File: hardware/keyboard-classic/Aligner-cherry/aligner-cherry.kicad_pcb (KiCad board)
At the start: 2 copper layers, 312.4 x 118.1 mm, 77 parts, among them SW1 RT Arrow, SW10 Bracket_Open, SW11 6, SW12 Y, SW13 Return, SW14 Dash, SW15 5, SW16 T, SW17 Line Feed, SW18 Colon, SW19 4, SW2 LT Arrow, SW20 R, SW21 O, SW22 0, SW23 3, SW24 E, SW25 L, SW26 9, SW27 2, SW28 W, SW29 Period, SW3 Tilde, SW30 8, SW31 1, SW32 @ (AT), SW33 Break, SW34 Rubout, SW35 R_Shift, SW36 P, SW37 Comma, SW38 K, SW39 L_Shift, SW4 I, SW40 Semicolon, SW41 M, SW42 J, SW43 Fwd_Slash, SW44 N, SW45 H, SW46 SPACE, SW47 B, SW48 G, SW49 TAB, SW5 Repeat, SW50 Z, SW51 V, SW52 F, SW53 CTRL, SW54 A, SW55 C, SW56 D, SW57 Backslash, SW58 Q, SW59 X, SW6 Bracket_Close, SW60 S, SW61 FN, SW62 ESC, SW7 7, SW8 U, SW9 Caps Lock

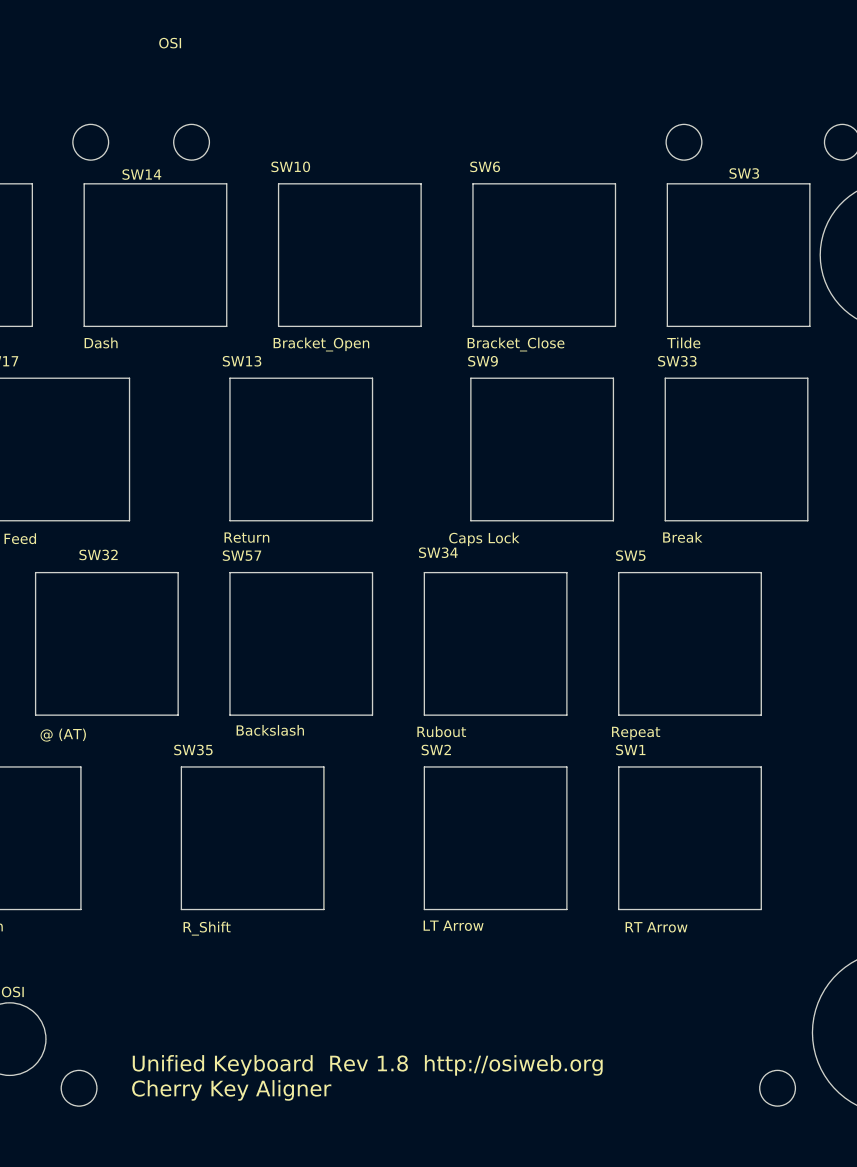
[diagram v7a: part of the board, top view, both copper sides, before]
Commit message: Adjust some holes so interface mount holes double as aligner mounts.
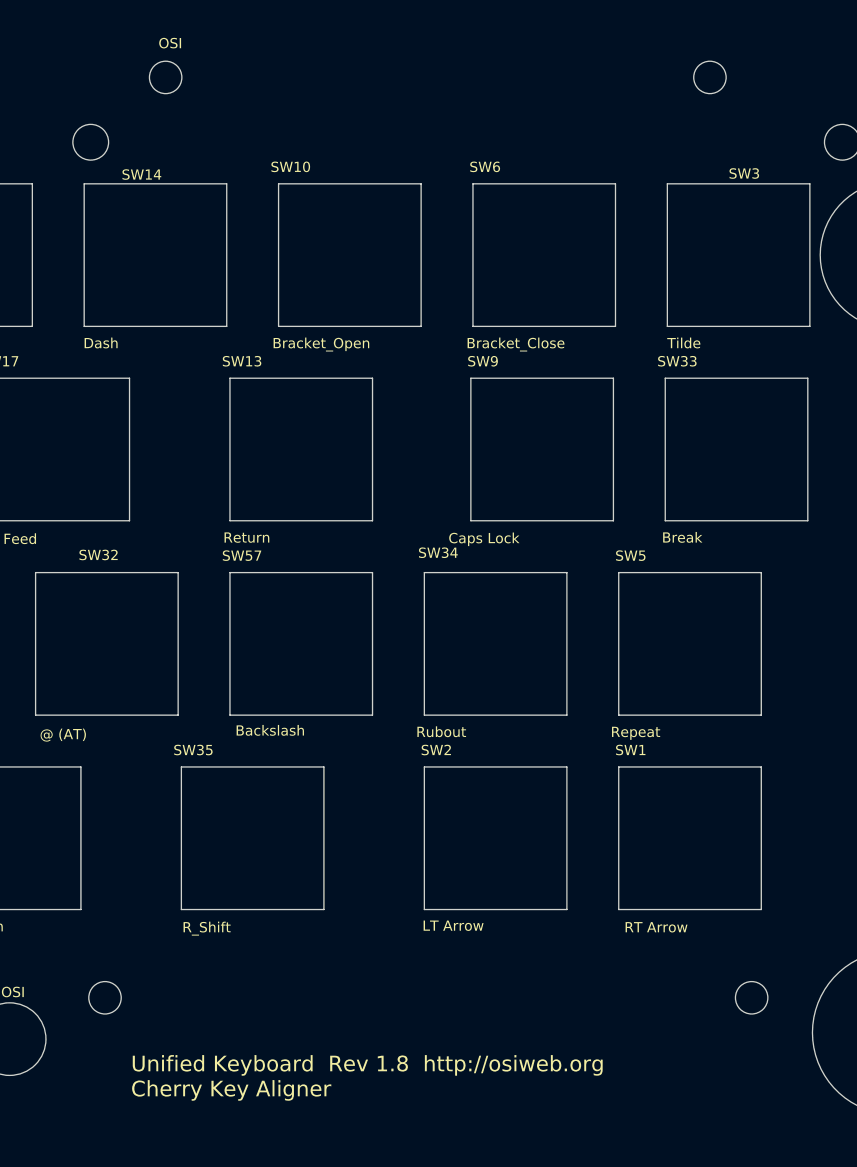
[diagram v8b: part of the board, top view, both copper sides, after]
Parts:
- removed the REF** at (349.0, 78.7)
- removed the REF** at (300.7, 78.7)
- removed the REF** at (358.1, 171.4)
- removed the REF** at (289.7, 171.4)
- added REF**: Interface mount, unikbd:kbd_mounting_holes_only, F.Cu at (301.0, 163.9)
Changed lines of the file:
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@@
     (tracks 0)
     (zones 0)
-    (modules 77)
+    (modules 74)
     (nets 1)
   )
@@
     (diff_pair_gap 0.254)
   )
+  (module unikbd:kbd_mounting_holes_only (layer F.Cu)
+    (at 301.0408 163.87826 90)
+    (descr "Through hole straight pin header, 2x20, 2.54mm pitch, double rows")
+    (tags "Through hole pin header THT 2x20 2.54mm double row")
+    (fp_text reference REF** (at 1.2954 -2.5078 90) (layer F.Fab) hide
+      (effects (font (size 1 1) (thickness 0.15)))
+    )
+    (fp_text value "Interface mount" (at 1.27 50.59 90) (layer F.Fab) hide
+      (effects (font (size 1 1) (thickness 0.15)))
+    )
+    (pad "" np_thru_hole circle (at 1.2954 54.5606 90) (size 3.175 3.175) (drill 3.175) (layers *.Cu *.Mask))
+    (pad "" np_thru_hole circle (at 1.2954 -8.8124 90) (size 3.175 3.175) (drill 3.175) (layers *.Cu *.Mask))
+    (pad "" np_thru_hole circle (at 91.4924 -2.8688 90) (size 3.175 3.175) (drill 3.175) (layers *.Cu *.Mask))
+    (pad "" np_thru_hole circle (at 91.4924 50.4712 90) (size 3.175 3.175) (drill 3.175) (layers *.Cu *.Mask))
+    (model ${KISYS3DMOD}/Connector_PinHeader_2.54mm.3dshapes/PinHeader_2x20_P2.54mm_Vertical.wrl
+      (offset (xyz 2.54 0 -1.8288))
+      (scale (xyz 1 1 1))
+      (rotate (xyz 0 180 0))
+    )
+  )
   (module unikbd:OSI_spacer_holes (layer F.Cu)
     (at 197.15988 165.99916)
@@
       (effects (font (size 1 1) (thickness 0.15)))
     )
+    (fp_line (start 104.14 -87.63) (end 104.14 -102.87) (layer F.CrtYd) (width 0.12))
+    (fp_line (start 104.14 -87.63) (end 114.3 -87.63) (layer F.CrtYd) (width 0.12))
+    (fp_line (start 114.3 -102.87) (end 114.3 -87.63) (layer F.CrtYd) (width 0.12))
+    (fp_line (start 104.14 -102.87) (end 114.3 -102.87) (layer F.CrtYd) (width 0.12))
+    (fp_line (start -114.3 -87.63) (end -114.3 -102.87) (layer F.CrtYd) (width 0.12))
+    (fp_line (start -114.3 -87.63) (end -104.14 -87.63) (layer F.CrtYd) (width 0.12))
+    (fp_line (start -104.14 -102.87) (end -104.14 -87.63) (layer F.CrtYd) (width 0.12))
+    (fp_line (start -114.3 -102.87) (end -104.14 -102.87) (layer F.CrtYd) (width 0.12))
+    (fp_line (start -5.08 -87.7824) (end -5.08 -103.0224) (layer F.CrtYd) (width 0.12))
+    (fp_line (start -5.08 -87.7824) (end 5.08 -87.7824) (layer F.CrtYd) (width 0.12))
+    (fp_line (start 5.08 -103.0224) (end 5.08 -87.7824) (layer F.CrtYd) (width 0.12))
+    (fp_line (start -5.08 -103.0224) (end 5.08 -103.0224) (layer F.CrtYd) (width 0.12))
+    (fp_circle (center 109.22 -97.79) (end 114.046 -97.79) (layer Cmts.User) (width 0.15))
+    (fp_circle (center -109.22 -97.79) (end -104.394 -97.79) (layer Cmts.User) (width 0.15))
+    (fp_circle (center 0 -97.9424) (end 4.826 -97.9424) (layer Cmts.User) (width 0.15))
+    (fp_circle (center -85.725 0.635) (end -81.975 0.635) (layer F.CrtYd) (width 0.05))
+    (fp_circle (center -85.725 0.635) (end -82.225 0.635) (layer Cmts.User) (width 0.15))
+    (fp_circle (center 85.725 0.635) (end 89.475 0.635) (layer F.CrtYd) (width 0.05))
+    (fp_circle (center 85.725 0.635) (end 89.225 0.635) (layer Cmts.User) (width 0.15))
+    (fp_circle (center 0 -92.8624) (end 4.826 -92.8624) (layer Cmts.User) (width 0.15))
+    (fp_circle (center -109.22 -92.71) (end -104.394 -92.71) (layer Cmts.User) (width 0.15))
     (fp_circle (center 109.22 -92.71) (end 114.046 -92.71) (layer Cmts.User) (width 0.15))
-    (fp_circle (center 109.22 -92.71) (end 114.3 -92.71) (layer F.CrtYd) (width 0.05))
-    (fp_circle (center -109.22 -92.71) (end -104.394 -92.71) (layer Cmts.User) (width 0.15))
-    (fp_circle (center -109.22 -92.71) (end -104.14 -92.71) (layer F.CrtYd) (width 0.05))
-    (fp_circle (center 0 -92.8624) (end 4.826 -92.8624) (layer Cmts.User) (width 0.15))
-    (fp_circle (center 0 -92.8624) (end 5.08 -92.8624) (layer F.CrtYd) (width 0.05))
-    (fp_circle (center 85.725 0.635) (end 89.225 0.635) (layer Cmts.User) (width 0.15))
-    (fp_circle (center 85.725 0.635) (end 89.475 0.635) (layer F.CrtYd) (width 0.05))
-    (fp_circle (center -85.725 0.635) (end -82.225 0.635) (layer Cmts.User) (width 0.15))
-    (fp_circle (center -85.725 0.635) (end -81.975 0.635) (layer F.CrtYd) (width 0.05))
-    (fp_circle (center 0 -97.9424) (end 4.826 -97.9424) (layer Cmts.User) (width 0.15))
-    (fp_circle (center 0 -97.9424) (end 5.08 -97.9424) (layer F.CrtYd) (width 0.05))
-    (fp_circle (center -109.22 -97.79) (end -104.394 -97.79) (layer Cmts.User) (width 0.15))
-    (fp_circle (center -109.22 -97.79) (end -104.14 -97.79) (layer F.CrtYd) (width 0.05))
-    (fp_circle (center 109.22 -97.79) (end 114.046 -97.79) (layer Cmts.User) (width 0.15))
-    (fp_circle (center 109.22 -97.79) (end 114.3 -97.79) (layer F.CrtYd) (width 0.05))
     (fp_text user %R (at 110.75162 -87.97036) (layer F.Fab)
       (effects (font (size 1 1) (thickness 0.15)))
@@
   )
   (module MountingHole:MountingHole_3.5mm (layer F.Cu)
-    (at 358.14 171.45)
-    (descr "Mounting Hole 3.5mm, no annular")
-    (tags "mounting hole 3.5mm no annular")
-    (attr virtual)
-    (fp_text reference REF** (at 0 -4.5) (layer F.SilkS) hide
-      (effects (font (size 1 1) (thickness 0.15)))
-    )
-    (fp_text value MountingHole_3.5mm (at 0 4.5) (layer F.Fab) hide
-      (effects (font (size 1 1) (thickness 0.15)))
-    )
-    (fp_circle (center 0 0) (end 3.5 0) (layer Cmts.User) (width 0.15))
-    (fp_circle (center 0 0) (end 3.75 0) (layer F.CrtYd) (width 0.05))
-    (fp_text user %R (at 0.3 0) (layer F.Fab) hide
-      (effects (font (size 1 1) (thickness 0.15)))
-    )
-    (pad 1 np_thru_hole circle (at 0 0) (size 3.5 3.5) (drill 3.5) (layers *.Cu *.Mask))
-  )
-  (module MountingHole:MountingHole_3.5mm (layer F.Cu)
-    (at 289.687 171.45)
-    (descr "Mounting Hole 3.5mm, no annular")
-    (tags "mounting hole 3.5mm no annular")
-    (attr virtual)
-    (fp_text reference REF** (at 0 -4.5) (layer F.SilkS) hide
-      (effects (font (size 1 1) (thickness 0.15)))
-    )
-    (fp_text value MountingHole_3.5mm (at 0 4.5) (layer F.Fab) hide
-      (effects (font (size 1 1) (thickness 0.15)))
-    )
-    (fp_circle (center 0 0) (end 3.5 0) (layer Cmts.User) (width 0.15))
-    (fp_circle (center 0 0) (end 3.75 0) (layer F.CrtYd) (width 0.05))
-    (fp_text user %R (at 0.3 0) (layer F.Fab) hide
-      (effects (font (size 1 1) (thickness 0.15)))
-    )
-    (pad 1 np_thru_hole circle (at 0 0) (size 3.5 3.5) (drill 3.5) (layers *.Cu *.Mask))
-  )
-  (module MountingHole:MountingHole_3.5mm (layer F.Cu)
     (at 364.49 78.74)
     (descr "Mounting Hole 3.5mm, no annular")
     (tags "mounting hole 3.5mm no annular")
-    (attr virtual)
-    (fp_text reference REF** (at 0 -4.5) (layer F.SilkS) hide
-      (effects (font (size 1 1) (thickness 0.15)))
-    )
-    (fp_text value MountingHole_3.5mm (at 0 4.5) (layer F.Fab) hide
-      (effects (font (size 1 1) (thickness 0.15)))
-    )
-    (fp_circle (center 0 0) (end 3.5 0) (layer Cmts.User) (width 0.15))
-    (fp_circle (center 0 0) (end 3.75 0) (layer F.CrtYd) (width 0.05))
-    (fp_text user %R (at 0.3 0) (layer F.Fab) hide
-      (effects (font (size 1 1) (thickness 0.15)))
-    )
-    (pad 1 np_thru_hole circle (at 0 0) (size 3.5 3.5) (drill 3.5) (layers *.Cu *.Mask))
-  )
-  (module MountingHole:MountingHole_3.5mm (layer F.Cu)
-    (at 348.9706 78.74)
-    (descr "Mounting Hole 3.5mm, no annular")
-    (tags "mounting hole 3.5mm no annular")
-    (attr virtual)
-    (fp_text reference REF** (at 0 -4.5) (layer F.SilkS) hide
-      (effects (font (size 1 1) (thickness 0.15)))
-    )
-    (fp_text value MountingHole_3.5mm (at 0 4.5) (layer F.Fab) hide
-      (effects (font (size 1 1) (thickness 0.15)))
-    )
-    (fp_circle (center 0 0) (end 3.5 0) (layer Cmts.User) (width 0.15))
-    (fp_circle (center 0 0) (end 3.75 0) (layer F.CrtYd) (width 0.05))
-    (fp_text user %R (at 0.3 0) (layer F.Fab) hide
-      (effects (font (size 1 1) (thickness 0.15)))
-    )
-    (pad 1 np_thru_hole circle (at 0 0) (size 3.5 3.5) (drill 3.5) (layers *.Cu *.Mask))
-  )
-  (module MountingHole:MountingHole_3.5mm (layer F.Cu)
-    (at 300.7106 78.74)
-    (descr "Mounting Hole 3.5mm, no annular")
-    (tags "mounting hole 3.5mm no annular")
